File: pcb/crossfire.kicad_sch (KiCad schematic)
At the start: 0 parts

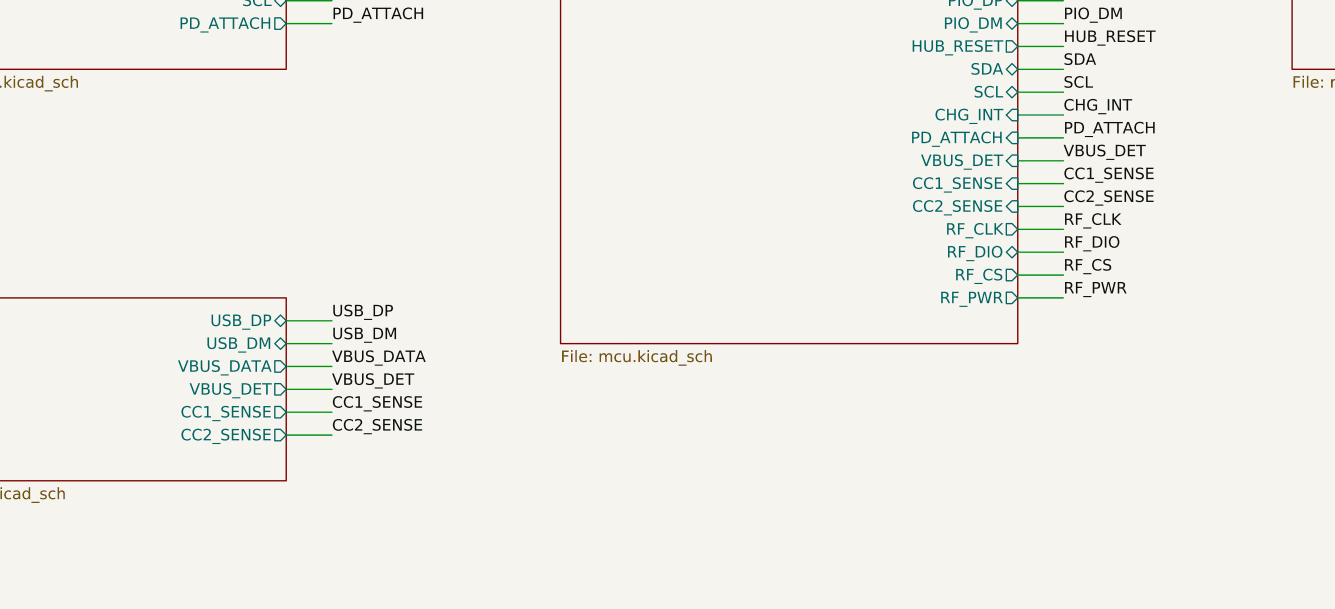
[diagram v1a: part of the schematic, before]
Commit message: take the CC senses out, and let that simplify what feeds the charger
Asking what the CC senses needed answered the question by deleting them. They
were there so the firmware could learn whether the data port's source offers
more than the USB default, but that buys nothing: the data port's contribution
is capped by intent rather than by what the source offers, because it exists so
a board with no battery and no charger can still be reflashed, not as a way to
run the ports. Removing them takes two pins, four resistors and a clamp
question off the board, and avoids a subtler risk -- any divider across CC sits
in parallel with the termination that tells the source what we are, and shifting
that is worse than not knowing.

Which collapses the ORing. A prioritised controller with external FETs was
specified because two sources meet at the charger and 9 V must never reach the
data port. A path limited to the USB default can afford a Schottky instead: it
blocks reverse without being told, costs about a fifth of a watt on a path that
is rarely used, and the charger's buck-boost input does not care about the drop.
The power port stays direct, on the condition that the sink opens its own output
switch when nothing is attached. The charger then tells its two sources apart by
their voltage, which it already measures, so the per-source limit is firmware
work rather than a board question.

The 9 V request is recorded from the driver in this codebase that already does
it on hardware: select the profile, then issue go, in that order, because go
acts on whatever the selection register holds at that instant -- and every
register written as a strictly framed two-byte transaction, because the
repeated-start form is acknowledged and stores nothing.

One new problem, found rather than closed. The port switch is rated 1.5 A and
goes constant-current near 2.15 A, so it protects the part but does not enforce
the port's budget; four of them could ask the 5 V rail for far more than it is
built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
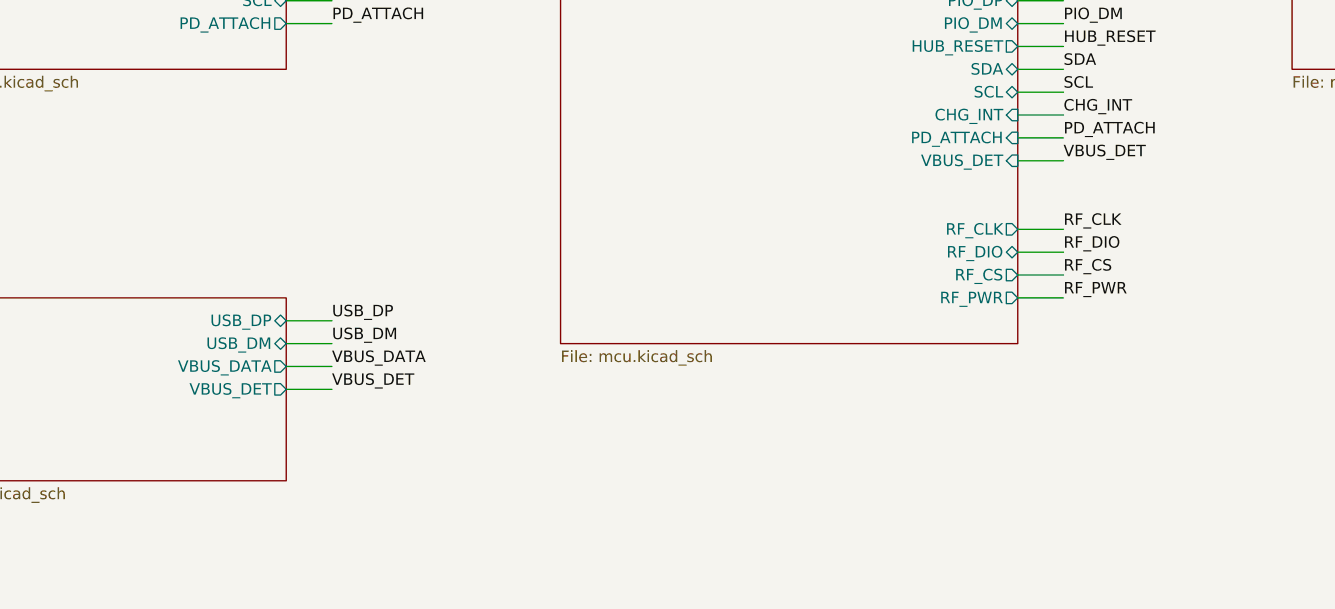
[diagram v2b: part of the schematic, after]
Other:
- sheet mcu ports: added none; removed CC1_SENSE, CC2_SENSE
- sheet upstream_data ports: added none; removed CC1_SENSE, CC2_SENSE
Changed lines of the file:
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@@
-	(wire
-		(pts
-			(xy 152.4 50.8) (xy 157.48 50.8)
-		)
-		(stroke
-			(width 0)
-			(type solid)
-		)
-	)
 	(wire
 		(pts
@@
 	(wire
 		(pts
-			(xy 152.4 48.26) (xy 157.48 48.26)
-		)
-		(stroke
-			(width 0)
-			(type solid)
-		)
-	)
-	(wire
-		(pts
 			(xy 325.12 104.14) (xy 330.2 104.14)
 		)
@@
 	(wire
 		(pts
-			(xy 71.12 76.2) (xy 76.2 76.2)
-		)
-		(stroke
-			(width 0)
-			(type solid)
-		)
-	)
-	(wire
-		(pts
 			(xy 152.4 116.84) (xy 157.48 116.84)
 		)
@@
 		(pts
 			(xy 152.4 43.18) (xy 157.48 43.18)
-		)
-		(stroke
-			(width 0)
-			(type solid)
-		)
-	)
-	(wire
-		(pts
-			(xy 71.12 73.66) (xy 76.2 73.66)
 		)
 		(stroke
@@
 		)
 	)
-	(label "CC1_SENSE"
-		(at 76.2 73.66 0)
-		(effects
-			(font
-				(size 1.27 1.27)
-			)
-			(justify left bottom)
-		)
-	)
 	(label "P2_DM"
 		(at 157.48 124.46 0)
@@
 		)
 	)
-	(label "CC2_SENSE"
-		(at 76.2 76.2 0)
-		(effects
-			(font
-				(size 1.27 1.27)
-			)
-			(justify left bottom)
-		)
-	)
 	(label "P3_PWR"
 		(at 157.48 137.16 0)
@@
 		)
 	)
-	(label "CC1_SENSE"
-		(at 157.48 48.26 0)
-		(effects
-			(font
-				(size 1.27 1.27)
-			)
-			(justify left bottom)
-		)
-	)
 	(label "RF_PWR"
 		(at 238.76 30.48 0)
@@
 	(label "P1_PWR"
 		(at 157.48 116.84 0)
-		(effects
-			(font
-				(size 1.27 1.27)
-			)
-			(justify left bottom)
-		)
-	)
-	(label "CC2_SENSE"
-		(at 157.48 50.8 0)
 		(effects
 			(font
@@
 			)
 		)
-		(pin "CC1_SENSE" input
-			(at 152.4 48.26 0)
-			(effects
-				(font
-					(size 1.27 1.27)
-				)
-				(justify right)
-			)
-		)
-		(pin "CC2_SENSE" input
-			(at 152.4 50.8 0)
-			(effects
-				(font
-					(size 1.27 1.27)
-				)
-				(justify right)
-			)
-		)
 		(pin "RF_CLK" output
 			(at 152.4 53.34 0)
@@
 			(effects
 				(font
-					(size 1.27 1.27)
-				)
-				(justify right)
-			)
-		)
-		(pin "CC1_SENSE" output
-			(at 71.12 73.66 0)
-			(effects
-				(font
-					(size 1.27 1.27)
-				)
-				(justify right)
-			)
-		)
-		(pin "CC2_SENSE" output
-			(at 71.12 76.2 0)
-			(effects
-				(font

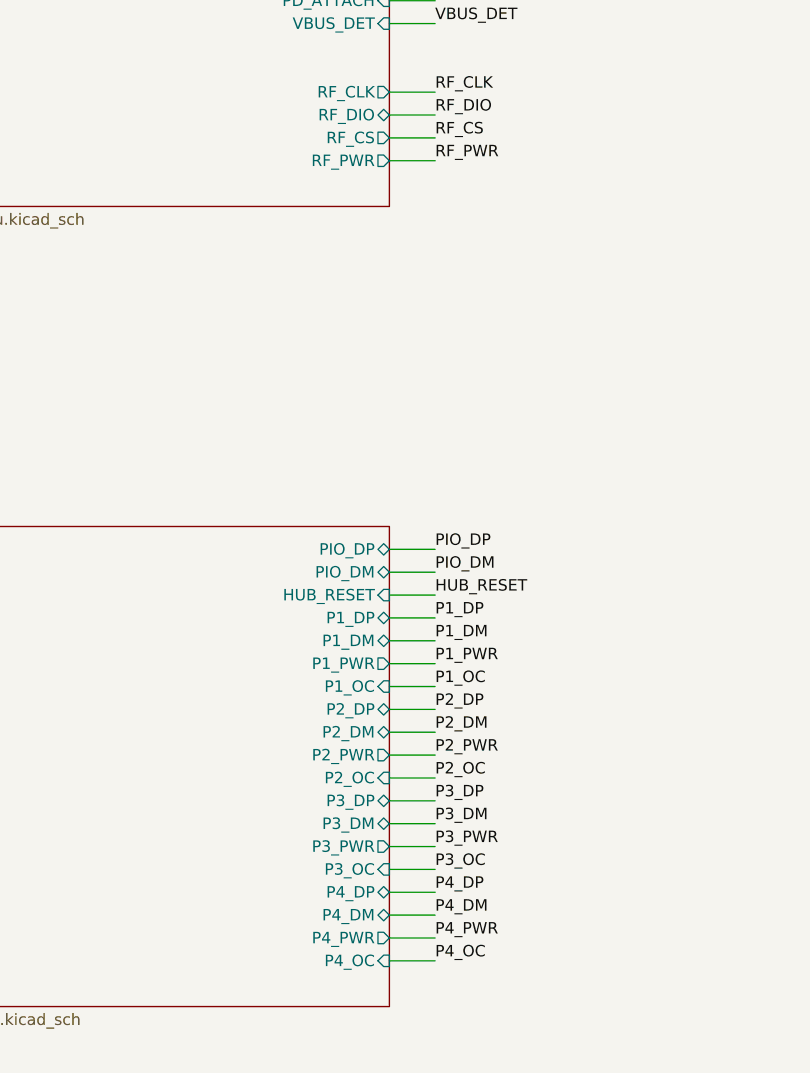
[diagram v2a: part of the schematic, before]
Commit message: draw the hub sheet, with every passive turned side-on
The hub, its 24 MHz crystal, the RBIAS reference, both regulator filters, the
straps that select the default configuration, the reset and upstream-detect
pull-downs, and the upstream pair's series resistors with their host-side
pull-downs.

The thing that makes this sheet readable is that the passives are rotated. A
part standing upright has to be reached by a wire that leaves its pin's row, and
on a chip with fourteen pins down one side those wires cross each other and
everything else. Turned side-on, each passive sits in line with the pin it
serves: every pin owns a row and nothing crosses. The rotation convention was
measured out of KiCad rather than assumed -- a symbol turned 90 degrees puts a
pin at (X - py, Y - px), and the pin's own direction turns with it.

The datasheet settled what hangs off each pin. Both regulator filters take up to
0.1uF to ground or may be left unconnected. RBIAS takes 12.0k at 1%. TEST is to
be left alone -- no trace, no signal. And the two configuration-select pins are
strapped low through resistors rather than tied, because after reset they revert
to other functions, one of them an output.

HUB_VBUS_DET is plumbed through: a sheet pin on both blocks in the root, and on
the MCU sheet a pin that was spare now drives it.

Co-Authored-By: Claude Opus 5 (1M context) <noreply@anthropic.com>
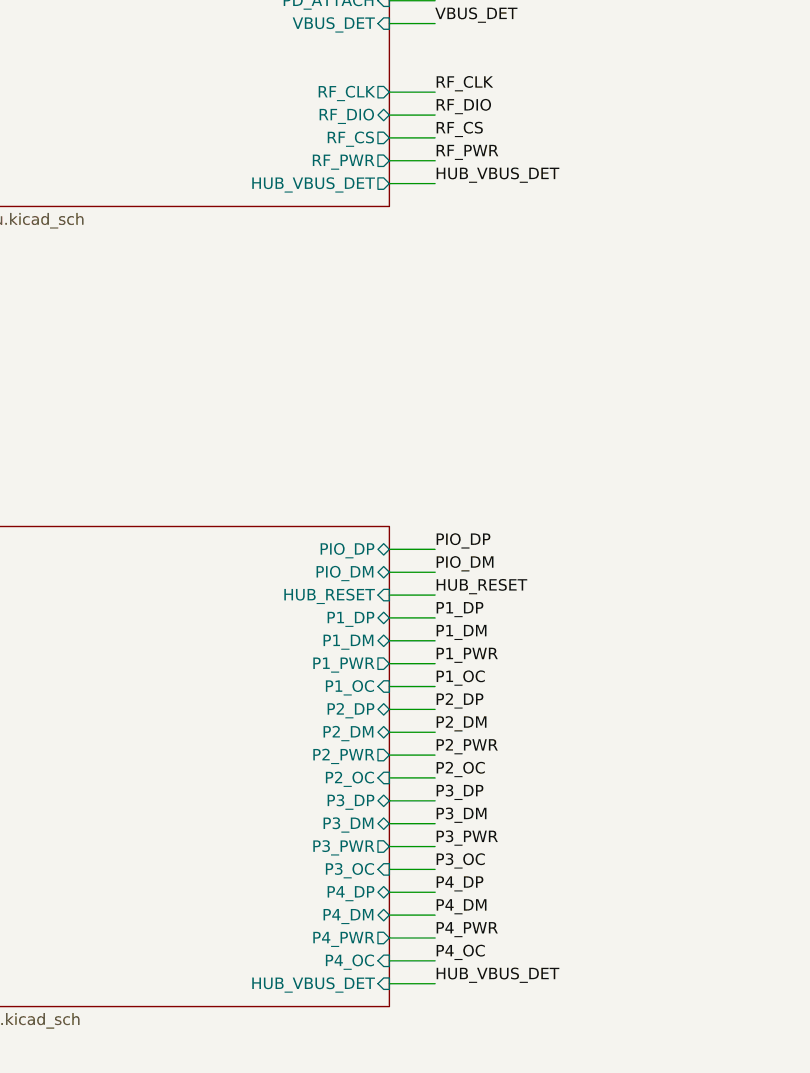
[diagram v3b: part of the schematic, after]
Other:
- sheet hub ports: added HUB_VBUS_DET; removed none
- sheet mcu ports: added HUB_VBUS_DET; removed none
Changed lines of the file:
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@@
 	(sheet
 		(at 101.6 20.32)
-		(size 50.8 45.72)
+		(size 50.80 45.72)
 		(exclude_from_sim no)
 		(in_bom yes)
@@
 		(pin "RF_PWR" output
 			(at 152.4 60.96 0)
+			(effects
+				(font
+					(size 1.27 1.27)
+				)
+				(justify right)
+			)
+		)
+		(pin "HUB_VBUS_DET" output
+			(at 152.40 63.50 0)
 			(effects
 				(font
@@
 	(sheet
 		(at 101.6 101.6)
-		(size 50.8 53.34)
+		(size 50.80 53.34)
 		(exclude_from_sim no)
 		(in_bom yes)
@@
 		(pin "P4_OC" input
 			(at 152.4 149.86 0)
+			(effects
+				(font
+					(size 1.27 1.27)
+				)
+				(justify right)
+			)
+		)
+		(pin "HUB_VBUS_DET" input
+			(at 152.40 152.40 0)
 			(effects
 				(font
@@
 	)
 	(embedded_fonts no)
+	(wire
+		(pts
+			(xy 152.40 63.50) (xy 157.48 63.50)
+		)
+		(stroke
+			(width 0)
+			(type solid)
+		)
+	)
+	(label "HUB_VBUS_DET"
+		(at 157.48 63.50 0)
+		(effects
+			(font
+				(size 1.27 1.27)
+			)
+			(justify left bottom)
+		)
+	)
+	(wire
+		(pts
+			(xy 152.40 152.40) (xy 157.48 152.40)
+		)
+		(stroke
+			(width 0)
+			(type solid)
+		)
+	)
+	(label "HUB_VBUS_DET"
+		(at 157.48 152.40 0)
+		(effects
+			(font
+				(size 1.27 1.27)
+			)
+			(justify left bottom)
+		)
+	)
 )

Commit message: draw the power port, and move its switch to the part that can drive it
The receptacle, the sink that negotiates on it, and its supply capacitor. The
terminations are inside the sink, so the configuration pins go straight across.
The bus pull-ups are not repeated here -- they live once, beside the charger.

Drawing it settled the open question about isolating this connector, and not the
way the question was framed. The sink has no output switch to open; it drives an
external one. But the charger already brings out a charge-pump drive for a
back-to-back pair on its own input, raises their gates above their common source
when the input is valid, and does the reverse blocking itself. That is the same
arrangement, from a part already in the design, with the gate drive and the
input-valid detection solved rather than designed. So the switch belongs beside
the charger, this sheet exports raw connector voltage, and the sink's gate output
goes unused.

The hardware attach signal comes out with it. The sink has no attach output, and
a plain divider cannot span five to nine volts into a three-and-a-quarter volt
input -- the ratio needed to read high at five is the one that reads over the
limit at nine. It was redundant anyway: the charger reports a valid input over
the same bus, and the sink's driver already reports the contract. That frees the
pin it held.

Co-Authored-By: Claude Opus 5 (1M context) <noreply@anthropic.com>
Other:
- sheet mcu ports: added none; removed PD_ATTACH
- sheet upstream_power ports: added none; removed PD_ATTACH
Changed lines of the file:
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@@
-	(wire
-		(pts
-			(xy 71.12 30.48) (xy 76.2 30.48)
-		)
-		(stroke
-			(width 0)
-			(type solid)
-		)
-	)
 	(wire
 		(pts
@@
 		(pts
 			(xy 254 111.76) (xy 259.08 111.76)
-		)
-		(stroke
-			(width 0)
-			(type solid)
-		)
-	)
-	(wire
-		(pts
-			(xy 152.4 43.18) (xy 157.48 43.18)
 		)
 		(stroke
@@
 		)
 	)
-	(label "PD_ATTACH"
-		(at 157.48 43.18 0)
-		(effects
-			(font
-				(size 1.27 1.27)
-			)
-			(justify left bottom)
-		)
-	)
 	(label "USB_DP"
 		(at 76.2 63.5 0)
@@
 	(label "P2_DP"
 		(at 330.2 104.14 0)
-		(effects
-			(font
-				(size 1.27 1.27)
-			)
-			(justify left bottom)
-		)
-	)
-	(label "PD_ATTACH"
-		(at 76.2 30.48 0)
 		(effects
 			(font
@@
 			)
 		)
-		(pin "PD_ATTACH" input
-			(at 152.4 43.18 0)
-			(effects
-				(font
-					(size 1.27 1.27)
-				)
-				(justify right)
-			)
-		)
 		(pin "VBUS_DET" input
 			(at 152.4 45.72 0)
@@
 			(effects
 				(font
-					(size 1.27 1.27)
-				)
-				(justify right)
-			)
-		)
-		(pin "PD_ATTACH" output
-			(at 71.12 30.48 0)
-			(effects
-				(font

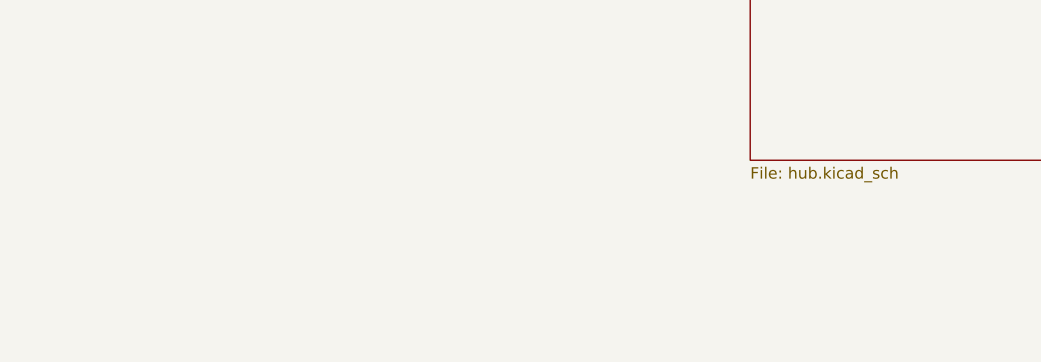
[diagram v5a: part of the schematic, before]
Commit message: give the board four mounting holes, in the drawing as well as on it
They are in the schematic because everything else on this board is, and a part that exists only on
the board is one that quietly disappears the next time the board is rebuilt from the drawing. Being
there also means they carry a net, which they need: these are plated and bonded to ground. Bonded
rather than bare because the asymmetry favours it -- five connector shells are already at ground, so
a metal enclosure's screw should join that system deliberately rather than through whatever it
touches, and against a plastic one the bond costs nothing. Leaving the pads off is the version that
cannot be undone without a new board.

Where they go was not a choice. Three of the four corners are inside a part: the bottom edge is four
sockets on a fixed pitch spanning nearly the full width, and the top right is the radio's clearance,
which a screw and its standoff have to respect as much as copper does. The positions are the point
furthest from the middle of the board in each quarter where a fastener actually fits, taking 8mm of
clear diameter, because an M3 head is 5.5mm and a washer 7mm and a hole only the drill clears is one
that cannot be done up. The search is against the outline polygon and the rule areas rather than a
rectangle, after a first attempt answered with two positions that overhung the rounded corners and
one that sat 0.15mm from the antenna's clearance.

Two consequences belong to the enclosure and are recorded rather than hidden. There is no hole
position anywhere in the lower left, because the power section fills it. And nothing comes within
16mm of the socket row, which is exactly where a plug is pushed in, so the enclosure has to carry
that row on a ledge rather than rely on these four screws.

One bug of mine on the way, worth naming because it is the same one that produced seventy annotation
errors before: the new ground symbols were numbered by scanning the sheet being edited, and power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
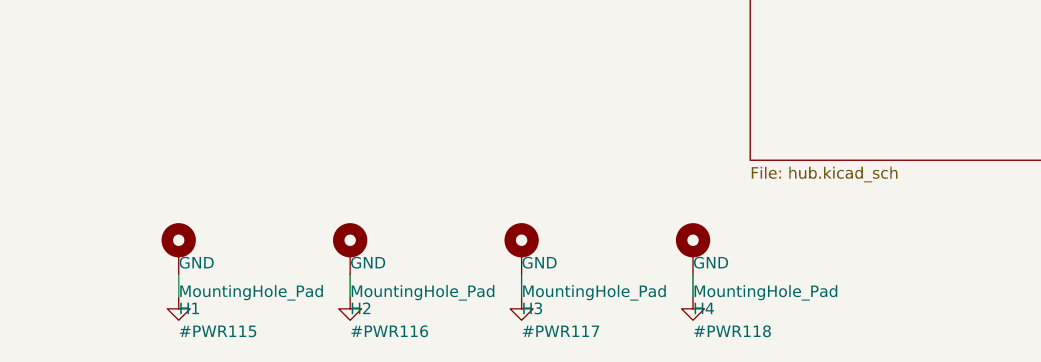
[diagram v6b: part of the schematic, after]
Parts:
- added H1, H2, H3, H4: MountingHole_Pad, MountingHole:MountingHole_3.2mm_M3_Pad, symbol Mechanical:MountingHole_Pad
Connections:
- new net GND: H1.1, H2.1, H3.1, H4.1

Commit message: checkpoint the battery, PD and radio design as it stood
The last state of the full-featured board before it is reduced to a single
USB-C input: the power block re-placed part by part in order of importance,
the charger's signal pins fanned out, the differential pairs renamed so the
layout tool recognises them, the 3.3 V converter's feedback divider joined
to its pin, the FETs given their part number, and the non-printing fields
hidden on the schematic. The layout is incomplete and is recorded as such.

Co-Authored-By: Claude Fable 5.1 <noreply@anthropic.com>
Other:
- sheet hub ports: added P1_D+, P1_D-, P2_D+, P2_D-, P3_D+, P3_D-, P4_D+, P4_D-, PIO_D+, PIO_D-; removed P1_DM, P1_DP, P2_DM, P2_DP, P3_DM, P3_DP, P4_DM, P4_DP, PIO_DM, PIO_DP
- sheet mcu ports: added PIO_D+, PIO_D-, USB_D+, USB_D-; removed PIO_DM, PIO_DP, USB_DM, USB_DP
- sheet port1 ports: added D+, D-; removed DM, DP
- sheet port2 ports: added D+, D-; removed DM, DP
- sheet port3 ports: added D+, D-; removed DM, DP
- sheet port4 ports: added D+, D-; removed DM, DP
- sheet upstream_data ports: added USB_D+, USB_D-; removed USB_DM, USB_DP
